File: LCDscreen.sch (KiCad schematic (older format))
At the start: 14 parts

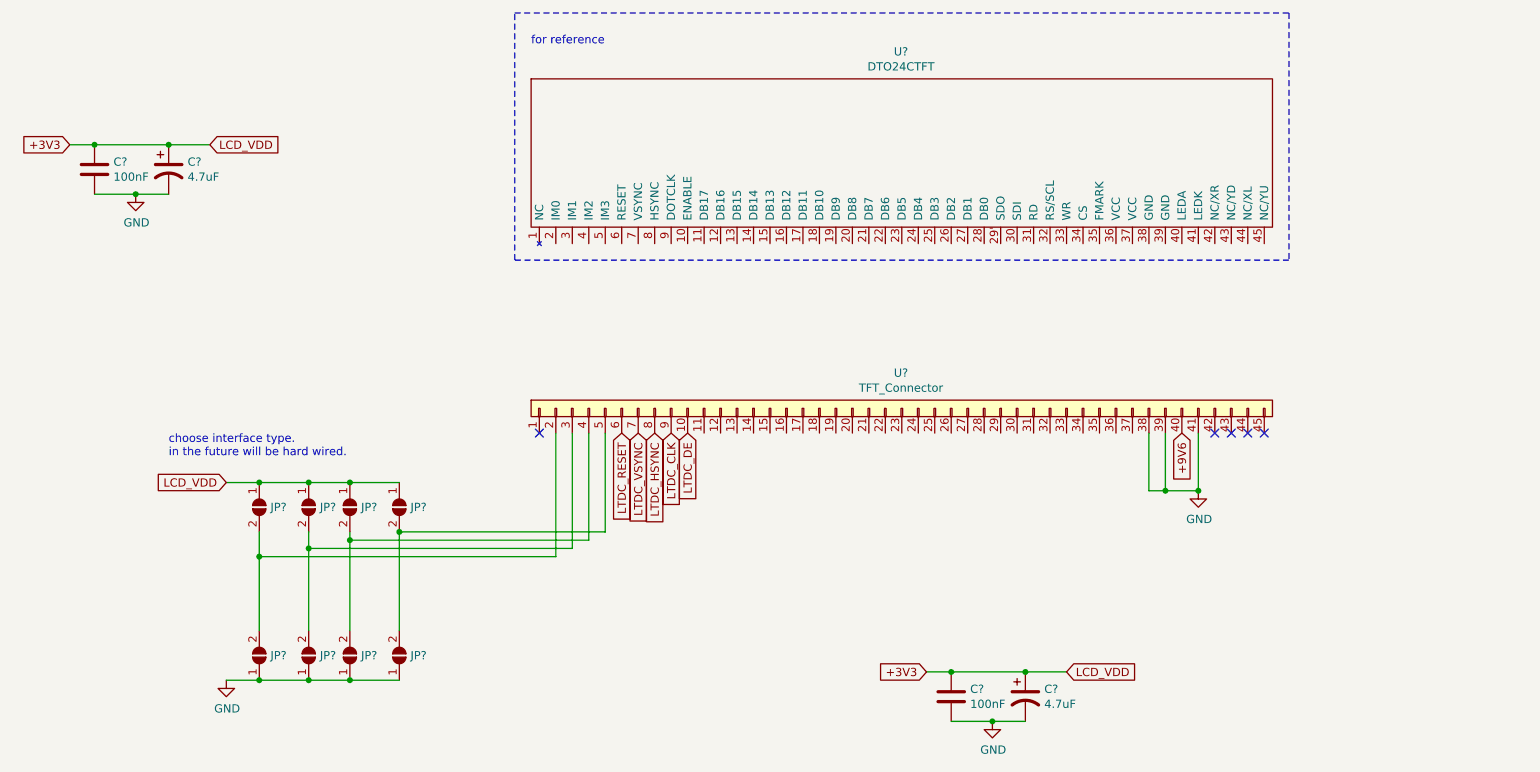
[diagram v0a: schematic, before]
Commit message: Finished adding LCD screen.
It turns out you also need to give it SPI so you can set it up.
We use the same SPI bus as the CODEC but give the display a chip-select pin.
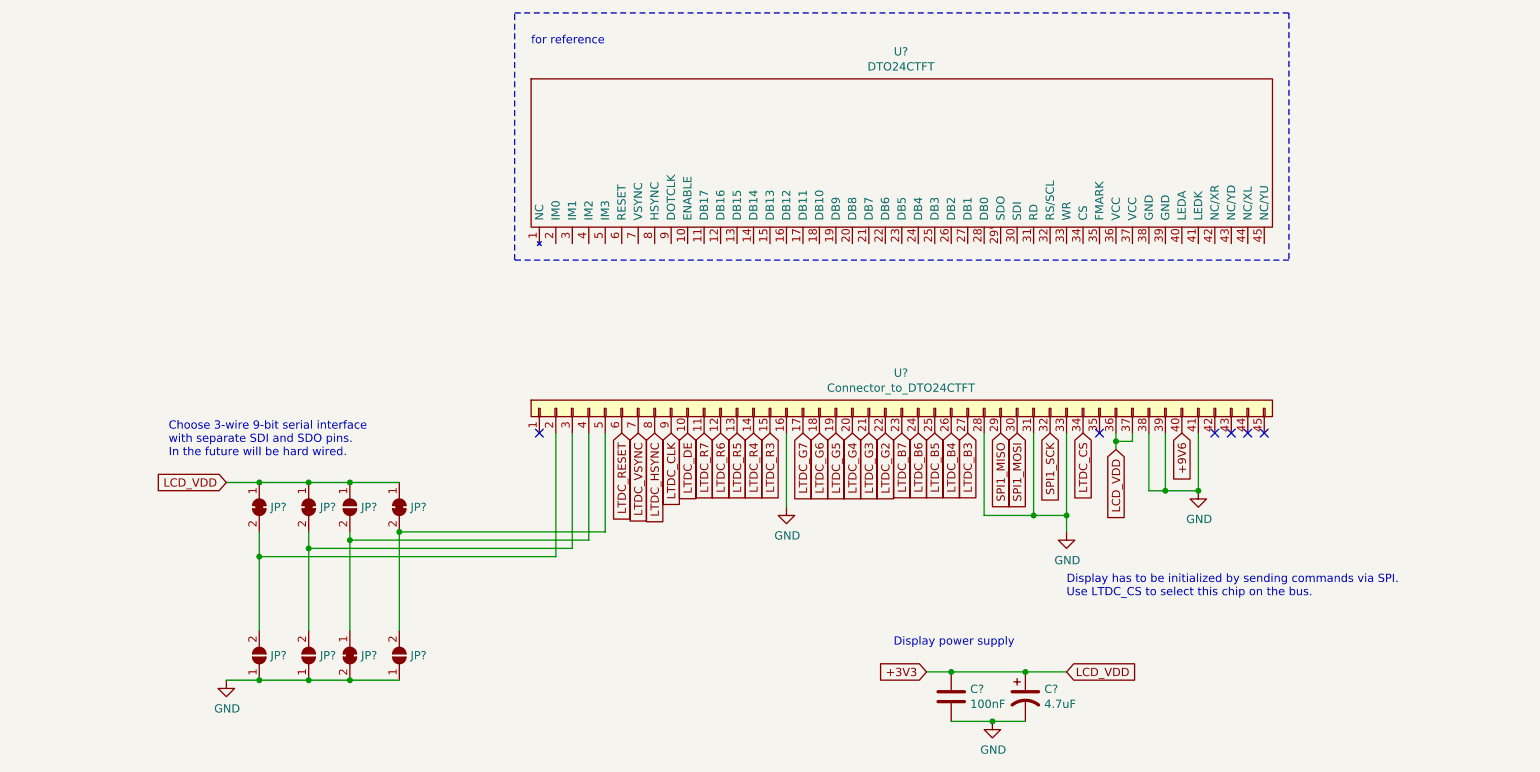
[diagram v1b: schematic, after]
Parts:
- removed C?: 100nF, symbol Device:C
- removed C?: 4.7uF, symbol Device:CP1
- removed JP? (x4): ~, symbol Jumper:SolderJumper_2_Open
- added JP? (x4): ~, symbol Jumper:SolderJumper_2_Bridged
- U?: value TFT_Connector -> Connector_to_DTO24CTFT
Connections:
- net +3V3: now also U?.36, U?.37, JP?.1 (A), JP?.1 (A), JP?.1 (A)
- net GND: now also U?.16, U?.28, U?.31, U?.33, JP?.2 (B)
- net LTDC_R7: now reaches U?.11
- net LTDC_R6: now reaches U?.12
- net LTDC_R5: now reaches U?.13
- net LTDC_R4: now reaches U?.14
- net LTDC_R3: now reaches U?.15
- net LTDC_G7: now reaches U?.17
- net LTDC_G6: now reaches U?.18
- net LTDC_G5: now reaches U?.19
- net at JP?.2 (B), U?.2: now also JP?.2 (B)
- net LTDC_G4: now reaches U?.20
- net LTDC_G3: now reaches U?.21
- net LTDC_G2: now reaches U?.22
- net LTDC_B7: now reaches U?.23
- net LTDC_B6: now reaches U?.24
- net LTDC_B5: now reaches U?.25
- net LTDC_B4: now reaches U?.26
- net LTDC_B3: now reaches U?.27
- net SPI1_MISO: now reaches U?.29
- net at JP?.2 (B), U?.3: now also JP?.2 (B)
- net SPI1_MOSI: now reaches U?.30
- net SPI1_SCK: now reaches U?.32
- net LTDC_CS: now reaches U?.34
- net at JP?.2 (B), U?.4: now also JP?.1 (A)
- net at JP?.2 (B), U?.5: now also JP?.2 (B)
- no-connect marks 5 -> 6
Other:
- note added: "Choose 3-wire 9-bit serial interface \nwith separate SDI and SDO pins.\nIn the future will be hard wired."
- note added: "Display has to be initialized by sending commands via SPI.\nUse LTDC_CS to select this chip on the bus."
- note added: "Display power supply"
- note removed: "choose interface type.\nin the future will be hard wired."
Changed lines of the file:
@@
 Comment4 ""
 $EndDescr
-Text GLabel 3450 1600 2    50   Input ~ 0
-LCD_VDD
-Text GLabel 2600 1600 0    50   Input ~ 0
-+3V3
-Wire Wire Line
-	2600 1600 2750 1600
-$Comp
-L power:GND #PWR?
-U 1 1 5CFECF09
-P 3000 1900
-AR Path="/5CFEB435/5CFECF09" Ref="#PWR?"  Part="1"
-AR Path="/5CFEBF88/5CFECF09" Ref="#PWR?"  Part="1"
-F 0 "#PWR?" H 3000 1650 50  0001 C CNN
-F 1 "GND" H 3005 1727 50  0000 C CNN
-F 2 "" H 3000 1900 50  0001 C CNN
-F 3 "" H 3000 1900 50  0001 C CNN
-	1    3000 1900
-	1    0    0    -1
-$EndComp
-$Comp
-L Device:C C?
-U 1 1 5CFECF0F
-P 2750 1750
-AR Path="/5CFEB435/5CFECF0F" Ref="C?"  Part="1"
-AR Path="/5CFEBF88/5CFECF0F" Ref="C?"  Part="1"
-F 0 "C?" H 2865 1796 50  0000 L CNN
-F 1 "100nF" H 2865 1705 50  0000 L CNN
-F 2 "" H 2788 1600 50  0001 C CNN
-F 3 "~" H 2750 1750 50  0001 C CNN
-	1    2750 1750
-	1    0    0    -1
-$EndComp
-$Comp
-L Device:CP1 C?
-U 1 1 5CFECF16
-P 3200 1750
-AR Path="/5CFEB435/5CFECF16" Ref="C?"  Part="1"
-AR Path="/5CFEBF88/5CFECF16" Ref="C?"  Part="1"
-F 0 "C?" H 3315 1796 50  0000 L CNN
-F 1 "4.7uF" H 3315 1705 50  0000 L CNN
-F 2 "" H 3200 1750 50  0001 C CNN
-F 3 "~" H 3200 1750 50  0001 C CNN
-	1    3200 1750
-	1    0    0    -1
-$EndComp
-Connection ~ 3200 1600
-Wire Wire Line
-	3200 1600 3450 1600
-Wire Wire Line
-	3000 1900 3200 1900
-Connection ~ 3000 1900
-Connection ~ 2750 1600
-Wire Wire Line
-	2750 1600 3200 1600
-Wire Wire Line
-	2750 1900 3000 1900
 $Comp
 L midi_studio_components:DTO24CTFT U?
@@
 P 7600 2950
 F 0 "U?" H 7645 2915 50  0000 C CNN
-F 1 "TFT_Connector" H 7645 2824 50  0000 C CNN
+F 1 "Connector_to_DTO24CTFT" H 7645 2824 50  0000 C CNN
 F 2 "" H 7600 2950 50  0001 C CNN
 F 3 "" H 7600 2950 50  0001 C CNN
@@
 $Comp
 L Jumper:SolderJumper_2_Open JP?
-U 1 1 5CFFFDD8
-P 3750 3800
-F 0 "JP?" V 3750 3868 50  0000 L CNN
-F 1 "~" V 3795 3868 50  0000 L CNN
-F 2 "" H 3750 3800 50  0001 C CNN
-F 3 "~" H 3750 3800 50  0001 C CNN
-	1    3750 3800
-	0    1    1    0
-$EndComp
-$Comp
-L Jumper:SolderJumper_2_Open JP?
-U 1 1 5CFFFE8F
-P 4050 3800
-F 0 "JP?" V 4050 3868 50  0000 L CNN
-F 1 "~" V 4095 3868 50  0000 L CNN
-F 2 "" H 4050 3800 50  0001 C CNN
-F 3 "~" H 4050 3800 50  0001 C CNN
-	1    4050 3800
-	0    1    1    0
-$EndComp
-$Comp
-L Jumper:SolderJumper_2_Open JP?
 U 1 1 5CFFFEB7
 P 4300 3800
@@
 	0    1    1    0
 $EndComp
-$Comp
-L Jumper:SolderJumper_2_Open JP?
-U 1 1 5CFFFEDD
-P 4600 3800
-F 0 "JP?" V 4600 3868 50  0000 L CNN
-F 1 "~" V 4645 3868 50  0000 L CNN
-F 2 "" H 4600 3800 50  0001 C CNN
-F 3 "~" H 4600 3800 50  0001 C CNN
-	1    4600 3800
-	0    1    1    0
-$EndComp
-Wire Wire Line
-	3550 3650 3750 3650
-Connection ~ 3750 3650
-Wire Wire Line
-	3750 3650 4050 3650
-Connection ~ 4050 3650
-Wire Wire Line
-	4050 3650 4300 3650
 Connection ~ 4300 3650
 Wire Wire Line
@@
 $Comp
 L Jumper:SolderJumper_2_Open JP?
-U 1 1 5D00155C
-P 4300 4700
-F 0 "JP?" V 4300 4768 50  0000 L CNN
-F 1 "~" V 4345 4768 50  0000 L CNN
-F 2 "" H 4300 4700 50  0001 C CNN
-F 3 "~" H 4300 4700 50  0001 C CNN
-	1    4300 4700
-	0    1    -1   0
-$EndComp
-$Comp
-L Jumper:SolderJumper_2_Open JP?
 U 1 1 5D001563
 P 4600 4700
@@
 	3750 4850 4050 4850
 Connection ~ 4050 4850
-Wire Wire Line
-	4050 4850 4300 4850
-Connection ~ 4300 4850
-Wire Wire Line
-	4300 4850 4600 4850
 $Comp
 L power:GND #PWR?
@@
 Wire Wire Line
 	4600 3950 4600 4550
-Connection ~ 4600 3950
 Text Notes 3200 3500 0    50   ~ 0
-choose interface type.\nin the future will be hard wired.
+Choose 3-wire 9-bit serial interface \nwith separate SDI and SDO pins.\nIn the future will be hard wired.
 Text GLabel 5950 3350 3    50   Input ~ 0
 LTDC_RESET
@@
 Text GLabel 6350 3350 3    50   Input ~ 0
 LTDC_DE
+$Comp
+L power:GND #PWR?
+U 1 1 5CFFF432
+P 6950 3800
+F 0 "#PWR?" H 6950 3550 50  0001 C CNN
+F 1 "GND" H 6955 3627 50  0000 C CNN
+F 2 "" H 6950 3800 50  0001 C CNN
+F 3 "" H 6950 3800 50  0001 C CNN
+	1    6950 3800
+	1    0    0    -1
+$EndComp
+Wire Wire Line
+	6950 3800 6950 3350
+Text GLabel 6450 3350 3    50   Input ~ 0
+LTDC_R7
+Text GLabel 6550 3350 3    50   Input ~ 0
+LTDC_R6
+Text GLabel 6650 3350 3    50   Input ~ 0
+LTDC_R5
+Text GLabel 6750 3350 3    50   Input ~ 0
+LTDC_R4
+Text GLabel 6850 3350 3    50   Input ~ 0
+LTDC_R3
+Text GLabel 7050 3350 3    50   Input ~ 0
+LTDC_G7
+Text GLabel 7150 3350 3    50   Input ~ 0
+LTDC_G6
+Text GLabel 7250 3350 3    50   Input ~ 0
+LTDC_G5
+Text GLabel 7350 3350 3    50   Input ~ 0
+LTDC_G4
+Text GLabel 7450 3350 3    50   Input ~ 0
+LTDC_G3
+Text GLabel 7550 3350 3    50   Input ~ 0
+LTDC_G2
+Text GLabel 7650 3350 3    50   Input ~ 0
+LTDC_B7
+Text GLabel 7750 3350 3    50   Input ~ 0
+LTDC_B6
+Text GLabel 7850 3350 3    50   Input ~ 0
+LTDC_B5
+Text GLabel 7950 3350 3    50   Input ~ 0
+LTDC_B4
+Text GLabel 8050 3350 3    50   Input ~ 0
+LTDC_B3
+NoConn ~ 8850 3350
+Text GLabel 8950 3450 3    50   Input ~ 0
+LCD_VDD
+Wire Wire Line
+	8950 3350 8950 3400
+Wire Wire Line
+	8950 3400 9050 3400
+Wire Wire Line
+	9050 3400 9050 3350
+Connection ~ 8950 3400
+Wire Wire Line
+	8950 3400 8950 3450
+Text GLabel 8750 3350 3    50   Input ~ 0
+LTDC_CS
+Text Notes 8650 4350 0    50   ~ 0
+Display has to be initialized by sending commands via SPI.\nUse LTDC_CS to select this chip on the bus.
+$Comp
+L power:GND #PWR?
+U 1 1 5D007F92
+P 8650 3950
+F 0 "#PWR?" H 8650 3700 50  0001 C CNN
+F 1 "GND" H 8655 3777 50  0000 C CNN
+F 2 "" H 8650 3950 50  0001 C CNN
+F 3 "" H 8650 3950 50  0001 C CNN
+	1    8650 3950
+	1    0    0    -1
+$EndComp
+Text GLabel 8250 3350 3    50   Input ~ 0
+SPI1_MISO
+Text GLabel 8350 3350 3    50   Input ~ 0
+SPI1_MOSI
+Text GLabel 8550 3350 3    50   Input ~ 0
+SPI1_SCK
+Wire Wire Line
+	8650 3350 8650 3850
+Wire Wire Line
+	8150 3350 8150 3850
+Wire Wire Line
+	8150 3850 8450 3850
+Connection ~ 8650 3850
+Wire Wire Line
+	8650 3850 8650 3950
+Wire Wire Line
+	8450 3350 8450 3850
+Connection ~ 8450 3850
+Wire Wire Line
+	8450 3850 8650 3850
+Wire Wire Line
+	3550 3650 3750 3650
+$Comp
+L Jumper:SolderJumper_2_Bridged JP?
+U 1 1 5D00F593
+P 3750 3800
+F 0 "JP?" V 3750 3868 50  0000 L CNN
+F 1 "~" V 3795 3868 50  0000 L CNN
+F 2 "" H 3750 3800 50  0001 C CNN
+F 3 "~" H 3750 3800 50  0001 C CNN
+	1    3750 3800
+	0    1    1    0
+$EndComp
+Connection ~ 3750 3650
+Wire Wire Line
+	3750 3650 4050 3650
+$Comp
+L Jumper:SolderJumper_2_Bridged JP?
+U 1 1 5D00FECF
+P 4050 3800
+F 0 "JP?" V 4050 3868 50  0000 L CNN
+F 1 "~" V 4095 3868 50  0000 L CNN
+F 2 "" H 4050 3800 50  0001 C CNN
+F 3 "~" H 4050 3800 50  0001 C CNN
+	1    4050 3800
+	0    1    1    0
+$EndComp
+Connection ~ 4050 3650
+Wire Wire Line
+	4050 3650 4300 3650
+Wire Wire Line
+	4050 4850 4300 4850
+$Comp
+L Jumper:SolderJumper_2_Bridged JP?
+U 1 1 5D00FF11
+P 4300 4700
+F 0 "JP?" V 4300 4768 50  0000 L CNN
+F 1 "~" V 4345 4768 50  0000 L CNN
+F 2 "" H 4300 4700 50  0001 C CNN
+F 3 "~" H 4300 4700 50  0001 C CNN
+	1    4300 4700
+	0    1    1    0
+$EndComp
+Connection ~ 4300 4850
+Wire Wire Line
+	4300 4850 4600 4850
+$Comp
+L Jumper:SolderJumper_2_Bridged JP?
+U 1 1 5D00FF77
+P 4600 3800
+F 0 "JP?" V 4600 3868 50  0000 L CNN
+F 1 "~" V 4645 3868 50  0000 L CNN
+F 2 "" H 4600 3800 50  0001 C CNN
+F 3 "~" H 4600 3800 50  0001 C CNN
+	1    4600 3800
+	0    1    1    0
+$EndComp
+Connection ~ 4600 3950
+Text Notes 7600 4650 0    50   ~ 0
+Display power supply
 $EndSCHEMATC
